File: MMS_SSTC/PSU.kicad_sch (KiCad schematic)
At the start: 18 parts, among them J1 Screw_Terminal_01x02, SW1 SW_SPST, U3 LM7812_TO220, U4 LM7805_TO220

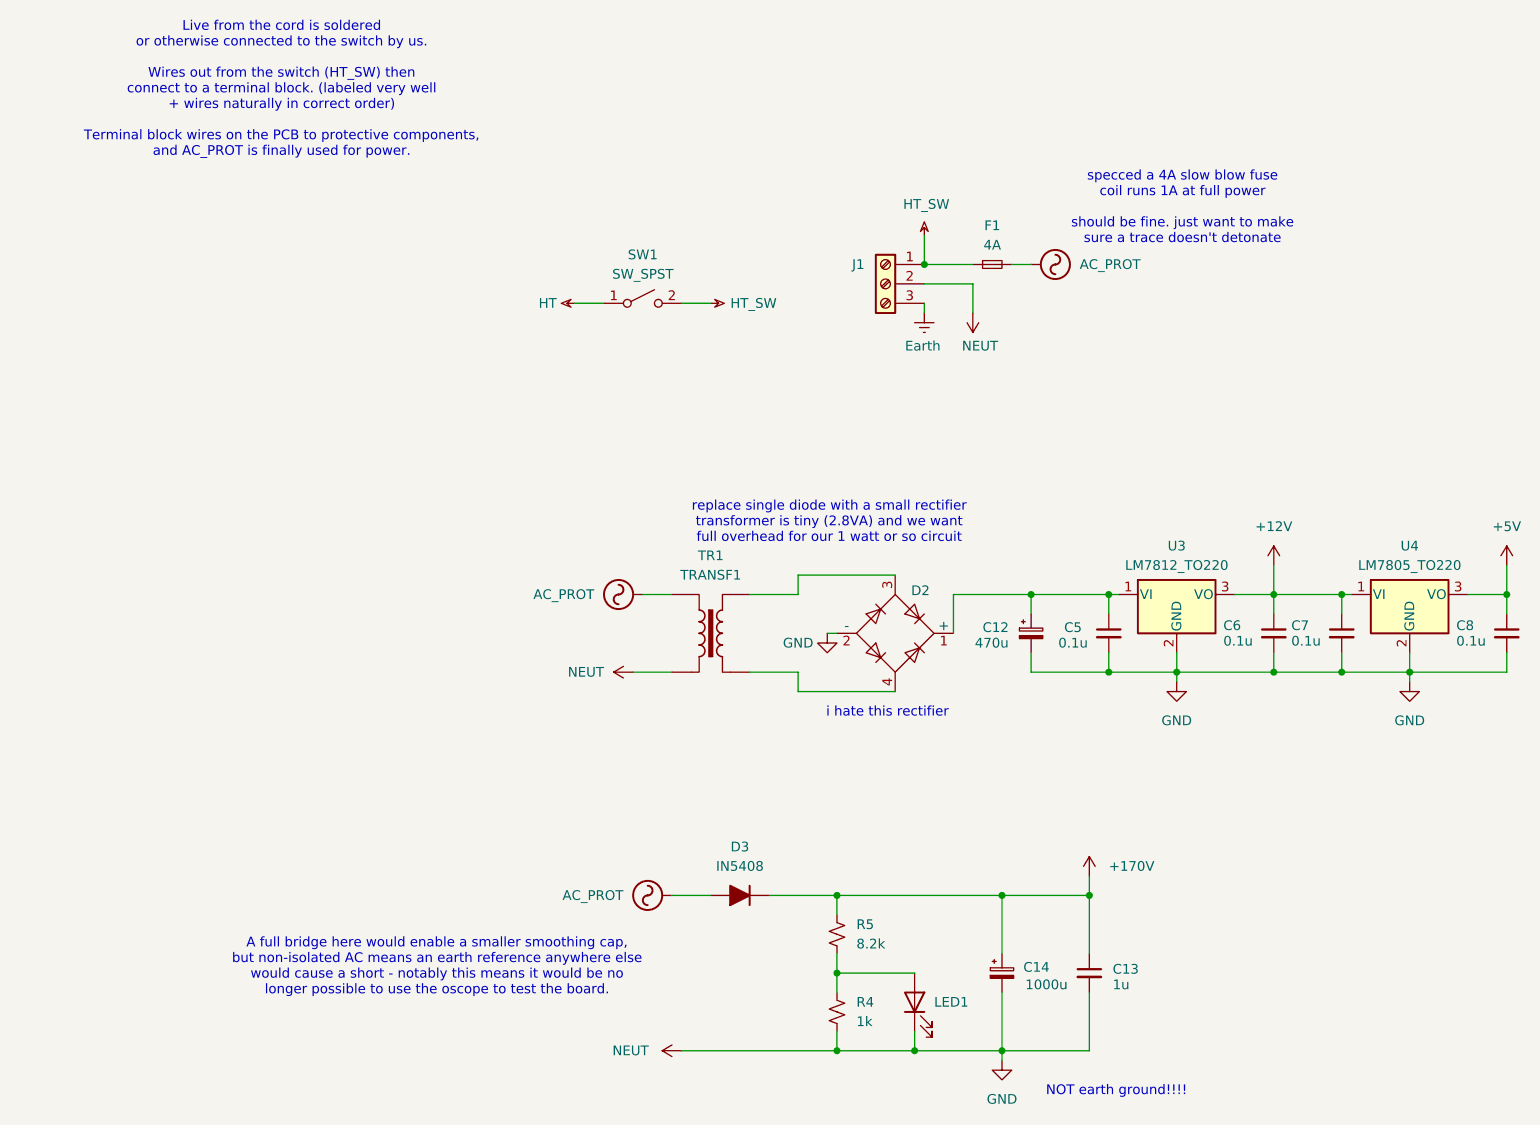
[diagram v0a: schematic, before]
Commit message: Update PCB trace clearances
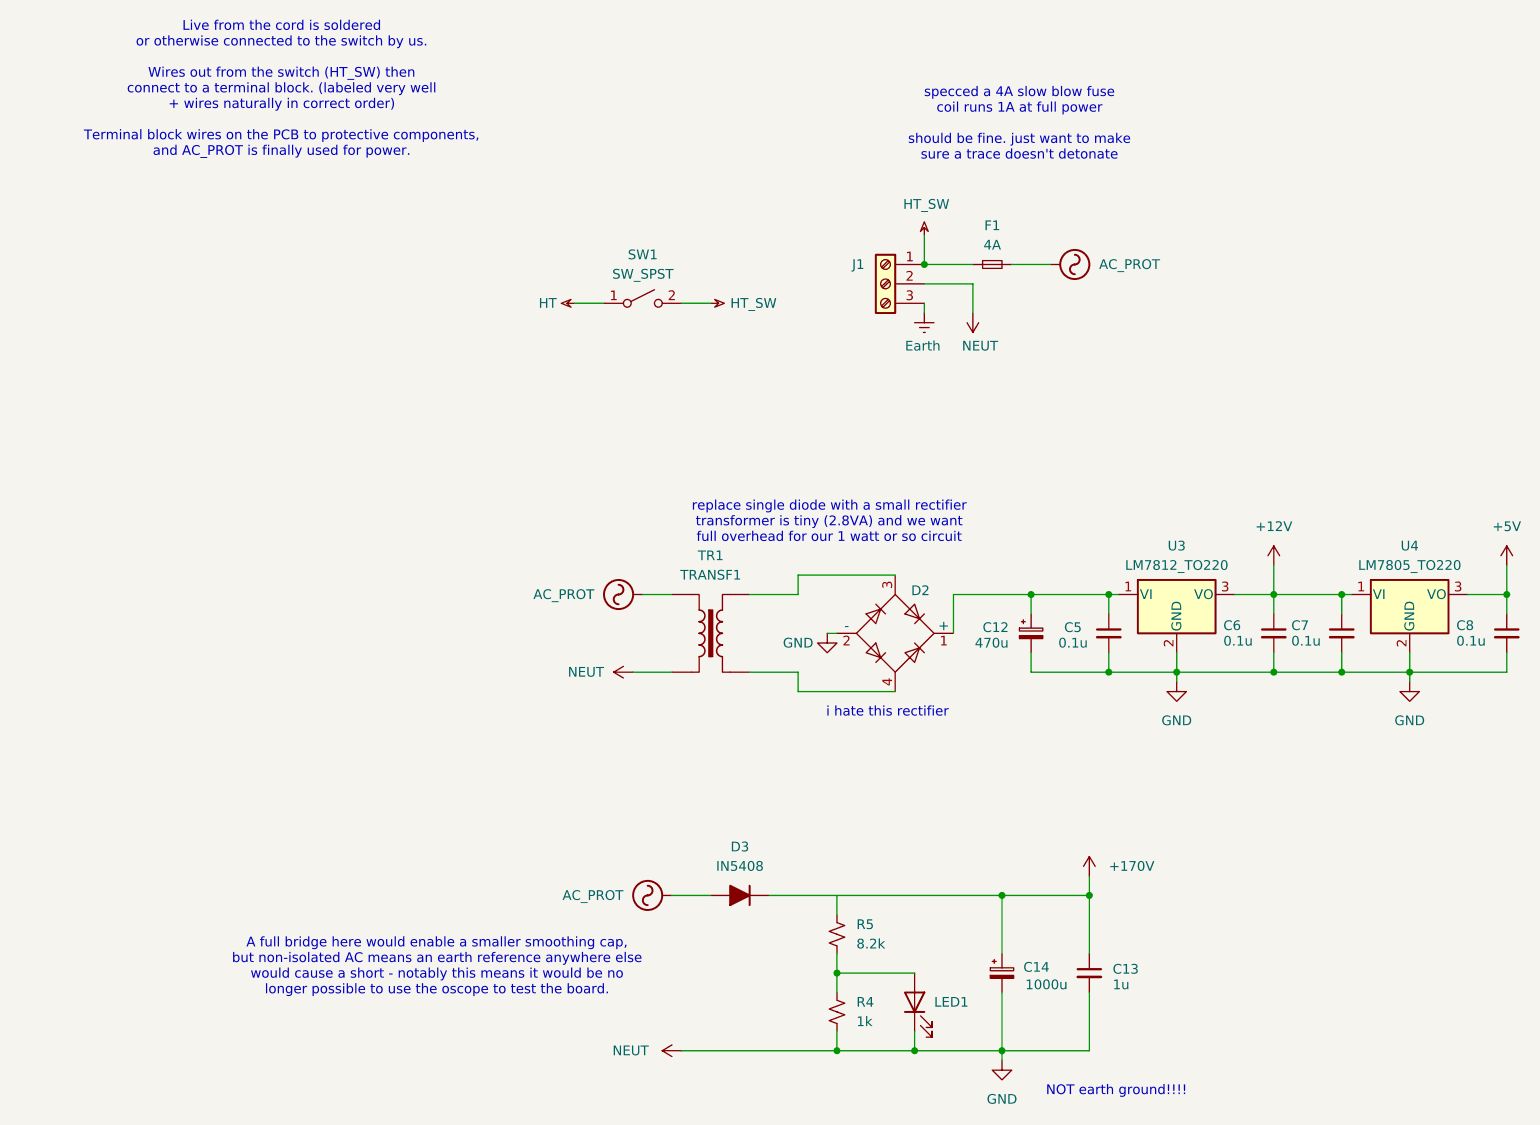
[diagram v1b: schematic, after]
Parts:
- LED1: footprint LED_THT:LED_D3.0mm -> LED_THT:LED_D5.0mm; DKPN 160-1603-ND -> 2007-BL-BBX1V4V-2-B02-ND; now in the parts list
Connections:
- net +170V: no longer R5.1
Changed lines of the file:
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@@
 	(text "specced a 4A slow blow fuse\ncoil runs 1A at full power\n\nshould be fine. just want to make \nsure a trace doesn't detonate"
 		(exclude_from_sim no)
-		(at 162.052 39.624 0)
+		(at 140.716 28.702 0)
 		(effects
 			(font
@@
 	)
 	(junction
-		(at 116.84 129.54)
-		(diameter 0)
-		(color 0 0 0 0)
-	)
-	(junction
 		(at 152.4 90.17)
 		(diameter 0)
@@
 	(wire
 		(pts
-			(xy 107.95 129.54) (xy 116.84 129.54)
+			(xy 107.95 129.54) (xy 138.43 129.54)
 		)
 		(stroke
@@
 	(wire
 		(pts
-			(xy 139.7 46.99) (xy 142.24 46.99)
+			(xy 139.7 46.99) (xy 144.78 46.99)
 		)
 		(stroke
@@
 	(wire
 		(pts
-			(xy 116.84 129.54) (xy 138.43 129.54)
-		)
-		(stroke
-			(width 0)
-			(type default)
-		)
-	)
-	(wire
-		(pts
 			(xy 204.47 86.36) (xy 204.47 90.17)
 		)
@@
 	)
 	(symbol
-		(lib_id "power:AC")
-		(at 142.24 46.99 270)
-		(unit 1)
-		(body_style 1)
-		(exclude_from_sim no)
-		(in_bom yes)
-		(on_board yes)
-		(in_pos_files yes)
-		(dnp no)
-		(fields_autoplaced yes)
-		(property "Reference" "#PWR031"
-			(at 139.7 46.99 0)
-			(hide yes)
-			(show_name no)
-			(do_not_autoplace no)
-			(effects
-				(font
-					(size 1.27 1.27)
-				)
-			)
-		)
-		(property "Value" "AC_PROT"
-			(at 148.59 46.9899 90)
-			(show_name no)
-			(do_not_autoplace no)
-			(effects
-				(font
-					(size 1.27 1.27)
-				)
-				(justify left)
-			)
-		)
-		(property "Footprint" ""
-			(at 142.24 46.99 0)
-			(hide yes)
-			(show_name no)
-			(do_not_autoplace no)
-			(effects
-				(font
-					(size 1.27 1.27)
-				)
-			)
-		)
-		(property "Datasheet" ""
-			(at 142.24 46.99 0)
-			(hide yes)
-			(show_name no)
-			(do_not_autoplace no)
-			(effects
-				(font
-					(size 1.27 1.27)
-				)
-			)
-		)
-		(property "Description" "Power symbol creates a global label with name \"AC\""
-			(at 142.24 46.99 0)
-			(hide yes)
-			(show_name no)
-			(do_not_autoplace no)
-			(effects
-				(font
-					(size 1.27 1.27)
-				)
-			)
-		)
-		(pin "1"
-		)
-		(instances
-			(project "MMS_SSTC"
-				(path "/b29a3901-c128-4c19-b69f-61de71283b43/bfaa6adf-6b83-46d0-b8b3-f415df3d6008"
-					(reference "#PWR031")
-					(unit 1)
-				)
-			)
-		)
-	)
-	(symbol
 		(lib_id "Connector:Screw_Terminal_01x03")
 		(at 123.19 49.53 0)
@@
 	)
 	(symbol
+		(lib_id "power:AC")
+		(at 91.44 90.17 90)
+		(unit 1)
+		(body_style 1)
+		(exclude_from_sim no)
+		(in_bom yes)
+		(on_board yes)
+		(in_pos_files yes)
+		(dnp no)
+		(fields_autoplaced yes)
+		(property "Reference" "#PWR035"
+			(at 93.98 90.17 0)
+			(hide yes)
+			(show_name no)
+			(do_not_autoplace no)
+			(effects
+				(font
+					(size 1.27 1.27)
+				)
+			)
+		)
+		(property "Value" "AC_PROT"
+			(at 85.09 90.1699 90)
+			(show_name no)
+			(do_not_autoplace no)
+			(effects
+				(font
+					(size 1.27 1.27)
+				)
+				(justify left)
+			)
+		)
+		(property "Footprint" ""
+			(at 91.44 90.17 0)
+			(hide yes)
+			(show_name no)
+			(do_not_autoplace no)
+			(effects
+				(font
+					(size 1.27 1.27)
+				)
+			)
+		)
+		(property "Datasheet" ""
+			(at 91.44 90.17 0)
+			(hide yes)
+			(show_name no)
+			(do_not_autoplace no)
+			(effects
+				(font
+					(size 1.27 1.27)
+				)
+			)
+		)
+		(property "Description" "Power symbol creates a global label with name \"AC\""
+			(at 91.44 90.17 0)
+			(hide yes)
+			(show_name no)
+			(do_not_autoplace no)
+			(effects
+				(font
+					(size 1.27 1.27)
+				)
+			)
+		)
+		(pin "1"
+		)
+		(instances
+			(project "MMS_SSTC"
+				(path "/b29a3901-c128-4c19-b69f-61de71283b43/bfaa6adf-6b83-46d0-b8b3-f415df3d6008"
+					(reference "#PWR035")
+					(unit 1)
+				)
+			)
+		)
+	)
+	(symbol
 		(lib_id "power:GND")
 		(at 115.57 95.25 0)
@@
 		(body_style 1)
 		(exclude_from_sim no)
-		(in_bom no)
+		(in_bom yes)
 		(on_board yes)
 		(in_pos_files yes)
@@
 			)
 		)
-		(property "Footprint" "LED_THT:LED_D3.0mm"
+		(property "Footprint" "LED_THT:LED_D5.0mm"
 			(at 127 143.51 0)
 			(hide yes)
@@
 			)
 		)
-		(property "DKPN" "160-1603-ND"
+		(property "DKPN" "2007-BL-BBX1V4V-2-B02-ND"
 			(at 127 143.51 90)
 			(hide yes)
@@
 			)
 		)
-		(property "Description" "Power symbol creates a global label with name \"+5V\""
+		(property "Description" "Power symbol creates a global label with name \"+170V\""
 			(at 149.86 127 0)
 			(hide yes)
@@
 	)
 	(symbol
+		(lib_id "power:AC")
+		(at 144.78 46.99 270)
+		(unit 1)
+		(body_style 1)
+		(exclude_from_sim no)
+		(in_bom yes)
+		(on_board yes)
+		(in_pos_files yes)
+		(dnp no)
+		(fields_autoplaced yes)
+		(property "Reference" "#PWR031"
+			(at 142.24 46.99 0)
+			(hide yes)
+			(show_name no)
+			(do_not_autoplace no)
+			(effects
+				(font
+					(size 1.27 1.27)
+				)
+			)
+		)
+		(property "Value" "AC_PROT"
+			(at 151.13 46.9899 90)
+			(show_name no)
+			(do_not_autoplace no)
+			(effects
+				(font
+					(size 1.27 1.27)
+				)
+				(justify left)
+			)
+		)
+		(property "Footprint" ""
+			(at 144.78 46.99 0)
+			(hide yes)
+			(show_name no)
+			(do_not_autoplace no)
+			(effects
+				(font
+					(size 1.27 1.27)
+				)
+			)
+		)
+		(property "Datasheet" ""
+			(at 144.78 46.99 0)
+			(hide yes)
+			(show_name no)
+			(do_not_autoplace no)
+			(effects
+				(font
+					(size 1.27 1.27)
+				)
+			)
+		)
+		(property "Description" "Power symbol creates a global label with name \"AC\""
+			(at 144.78 46.99 0)
+			(hide yes)
+			(show_name no)
+			(do_not_autoplace no)
+			(effects
+				(font
+					(size 1.27 1.27)
+				)
+			)
+		)
+		(pin "1"
+		)
+		(instances
+			(project "MMS_SSTC"
+				(path "/b29a3901-c128-4c19-b69f-61de71283b43/bfaa6adf-6b83-46d0-b8b3-f415df3d6008"
+					(reference "#PWR031")
+					(unit 1)
+				)
+			)
+		)
+	)
+	(symbol
 		(lib_id "Transformer:TRANSF1")
 		(at 100.33 95.25 0)
@@
 					(unit 1)
 				)
-			)
-		)
-	)
-	(symbol
-		(lib_id "power:AC")
-		(at 91.44 90.17 90)
-		(unit 1)
-		(body_style 1)
-		(exclude_from_sim no)
-		(in_bom yes)
-		(on_board yes)
-		(in_pos_files yes)
-		(dnp no)
-		(fields_autoplaced yes)
-		(property "Reference" "#PWR020"
-			(at 93.98 90.17 0)
-			(hide yes)
-			(show_name no)
-			(do_not_autoplace no)
-			(effects
-				(font
-					(size 1.27 1.27)
-				)
-			)
-		)
-		(property "Value" "AC_PROT"
-			(at 85.09 90.1699 90)
-			(show_name no)
-			(do_not_autoplace no)
-			(effects
-				(font
-					(size 1.27 1.27)
-				)
-				(justify left)
-			)
-		)
-		(property "Footprint" ""
-			(at 91.44 90.17 0)
-			(hide yes)
-			(show_name no)
-			(do_not_autoplace no)
-			(effects
-				(font
-					(size 1.27 1.27)
-				)
-			)
-		)
-		(property "Datasheet" ""
-			(at 91.44 90.17 0)
-			(hide yes)
-			(show_name no)
-			(do_not_autoplace no)
-			(effects
-				(font
-					(size 1.27 1.27)
-				)
-			)
-		)
-		(property "Description" "Power symbol creates a global label with name \"AC\""
-			(at 91.44 90.17 0)
-			(hide yes)
-			(show_name no)
-			(do_not_autoplace no)
-			(effects
-				(font
-					(size 1.27 1.27)
-				)
-			)
-		)
-		(pin "1"
-		)
-		(instances
-			(project "MMS_SSTC"
-				(path "/b29a3901-c128-4c19-b69f-61de71283b43/bfaa6adf-6b83-46d0-b8b3-f415df3d6008"
-					(reference "#PWR020")
-					(unit 1)
-				)

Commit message: Get CAD semi-finished, tweak PCB
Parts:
- renumbered C12 to C11, C13 to C12, C14 to C13
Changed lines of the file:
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@@
 		(in_pos_files yes)
 		(dnp no)
-		(property "Reference" "C14"
+		(property "Reference" "C13"
 			(at 141.224 138.938 0)
 			(show_name no)
@@
 			(project "MMS_SSTC"
 				(path "/b29a3901-c128-4c19-b69f-61de71283b43/bfaa6adf-6b83-46d0-b8b3-f415df3d6008"
-					(reference "C14")
+					(reference "C13")
 					(unit 1)
 				)
@@
 		(in_pos_files yes)
 		(dnp no)
-		(property "Reference" "C12"
+		(property "Reference" "C11"
 			(at 135.89 94.488 0)
 			(show_name no)
@@
 			(project "MMS_SSTC"
 				(path "/b29a3901-c128-4c19-b69f-61de71283b43/bfaa6adf-6b83-46d0-b8b3-f415df3d6008"
-					(reference "C12")
+					(reference "C11")
 					(unit 1)
 				)
@@
 		(in_pos_files yes)
 		(dnp no)
-		(property "Reference" "C13"
+		(property "Reference" "C12"
 			(at 152.908 139.192 0)
 			(show_name no)
@@
 			(project "MMS_SSTC"
 				(path "/b29a3901-c128-4c19-b69f-61de71283b43/bfaa6adf-6b83-46d0-b8b3-f415df3d6008"
-					(reference "C13")
-					(unit 1)
-				)
+					(reference "C12")
+					(unit 1)
+				)
